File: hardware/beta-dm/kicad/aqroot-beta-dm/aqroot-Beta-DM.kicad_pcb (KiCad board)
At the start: 4 copper layers, 74 x 155 mm, 188 parts, among them J1 CH280QV10-CT_50P, J2 Molex_5025700893, J3 USB_C_Receptacle_USB2.0_16P, J4 JST-PH-2 BATTERY, J5 COMMUNITY_HEADER_2x13, J6 JST-PH-2 SPEAKER, Q1 AO3400A, SW1 BOOT, SW2 UP, SW3 DOWN, SW4 LEFT, SW5 RIGHT, SW6 A_SELECT, SW7 B_BACK, SW8 HOME, SW9 SW_SPDT, U1 ESP32-S3-WROOM-1, U10 USBLC6-2SC6, U11 BQ25185, U12 TPS63020, U13 TPS61023, U14 MAX17048, U15 TPS22918, U16 TCA9517ADGK, U17 TPS61169DCKR, U2 TCA9535PWR, U3 TCA9535PWR, U4 BMI270, U5 MAX98357A, U6 TSOP38238, U7 E07-400M10S, U8 E22-900M22S, U9 ST25R3916-AQET

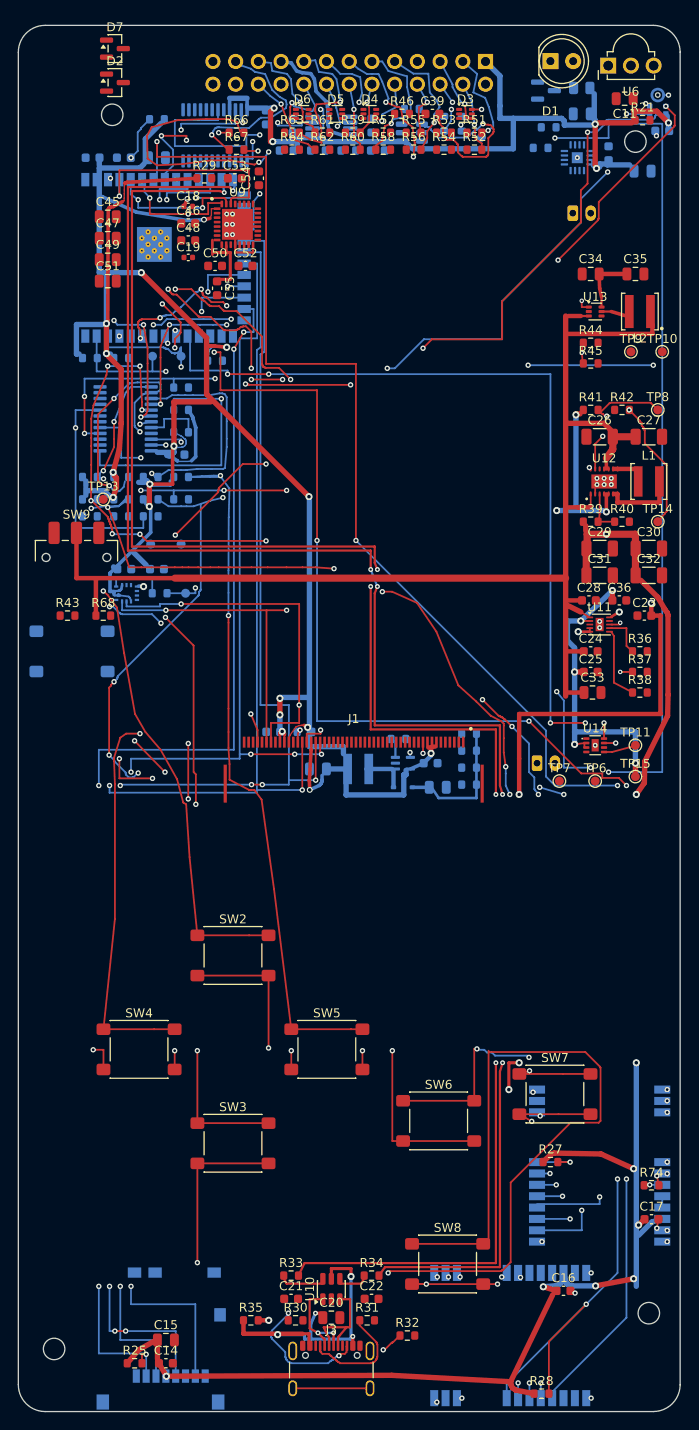
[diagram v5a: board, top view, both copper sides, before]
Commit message: hardware(beta-dm): GND stitching for the USB-C connector, the MCU and the switches
Copper. Only hardware/beta-dm/ is touched. Still no pours.

9 further stitches on grounds that gate a demo function rather than waiting for
the pour to find them:

  J3.A12   USB-C connector ground
  U1.1, U1.40   ESP32-S3 module grounds
  SW1.2    BOOT switch return
  R30.2, R31.2  the two 5.1k CC pull-downs - without these the Rd termination
                has no return and USB-C sink detection does not work
  R32.2    the 0R shield tie
  C1.1     the EN reset capacitor return
  R42.1    the PS_SYNC 0R tie to GND

Stub lengths 0.525-0.810 mm.

J3.B12 could not be stitched: no legal via site within 3.6 mm of it, the
connector corner is fully enclosed. It is an F.Cu ground pad, so the F.Cu pour
will pick it up when pours are created; it is recorded rather than forced.

Result: GND endpoints now 0 at U1, R30, R31, R32, C1 and R42; J3 1 (B12) and
SW1 2 remain for the pour. Board unconnected 239 -> 230.

Note on why these matter beyond tidiness. R30 and R31 are the USB-C CC
terminations - a 5.1k Rd with no ground return is not an Rd, and a source would
never see the sink. C1 is the ESP32-S3 reset capacitor and R42 ties the TPS63020
mode pin low; both are pull-to-ground parts whose function is exactly the
ground connection.

Verification: exact analytic validation - 0 violations, minimum separation
0.200 mm. Zones refilled through pcbnew, DRC 0 errors and 240 warnings with the
composition unchanged. Object-level preservation diff: 9 segments and 9 vias
added, 0 changes to footprints, pads, zones or Edge.Cuts. UUID prefix 9d54ba00,
verified absent before writing.

BETA FULL DIRECTORY: UNCHANGED.

Co-Authored-By: Claude Opus 5 <noreply@anthropic.com>
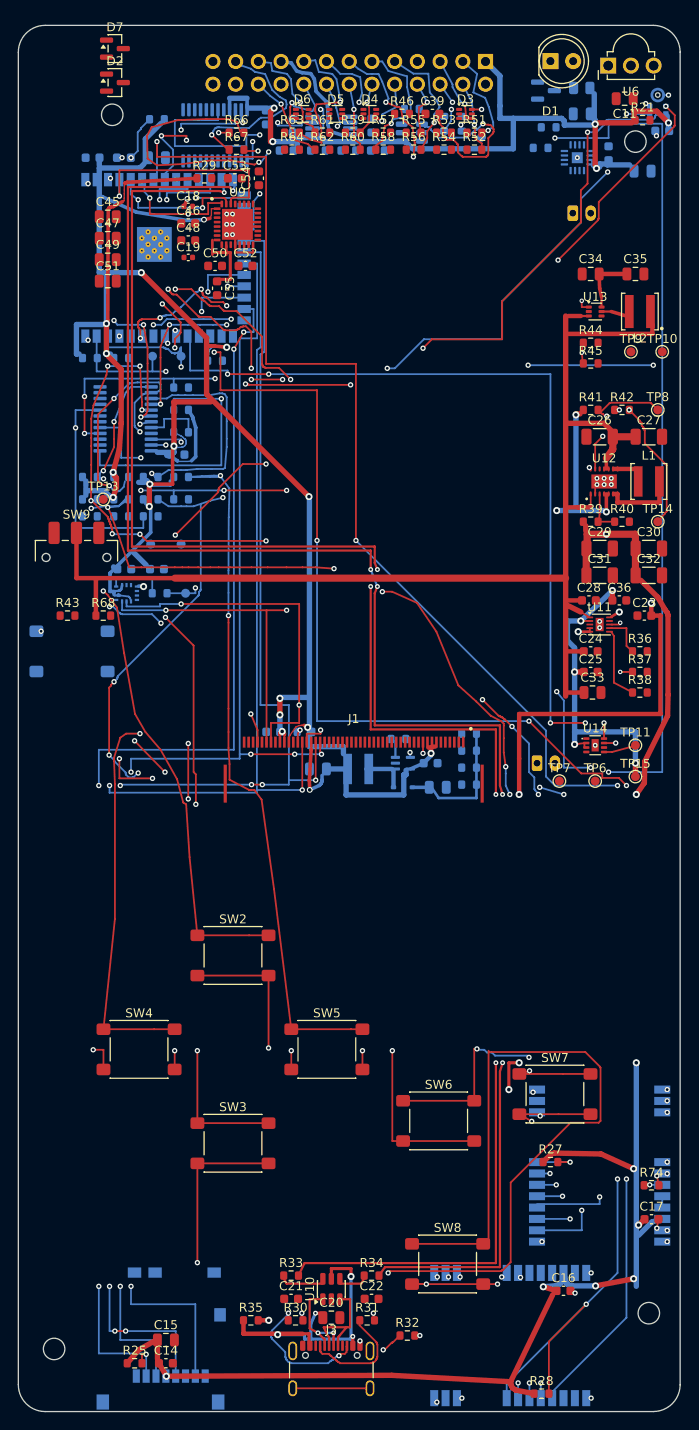
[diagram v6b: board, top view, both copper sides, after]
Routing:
- net GND: track 106.9 -> 112.4 mm, vias 52 -> 61
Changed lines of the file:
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@@
 	(footprint "C_0603_1608Metric"
 		(layer "B.Cu")
-		(at 28.5 79 180)
+		(at 46.1 82.5)
 		(descr "Capacitor SMD 0603 (1608 Metric), square (rectangular) end terminal, IPC-7351 nominal, (Body size source: IPC-SM-782 page 76, https://www.pcb-3d.com/wordpress/wp-content/uploads/ipc-sm-782a_amendment_1_and_2.pdf)")
 		(tags "capacitor")
-		(property "Reference" "C13"
-			(at 0 1.43 0)
+		(property "Reference" "C56"
+			(at 0 1.43 180)
 			(layer "B.SilkS")
 			(effects
@@
 			)
 		)
-		(property "Value" "100nF"
-			(at 0 -1.43 0)
+		(property "Value" "1uF"
+			(at 0 -1.43 180)
 			(layer "B.Fab")
 			(effects
@@
 		)
 		(property "Datasheet" ""
-			(at 0 0 0)
+			(at 0 0 180)
 			(layer "B.Fab")
 			(hide yes)
@@
 		)
 		(property "Description" ""
-			(at 0 0 0)
+			(at 0 0 180)
 			(layer "B.Fab")
 			(hide yes)
@@
 		)
 		(property "KiLib_Generator" "SMD_2terminal_chip_molded"
-			(at 0 0 0)
+			(at 0 0 180)
 			(layer "B.SilkS")
 			(hide yes)
@@
 		(duplicate_pad_numbers_are_jumpers no)
 		(fp_line
-			(start -0.14058 0.51)
-			(end 0.14058 0.51)
+			(start -0.14058 -0.51)
+			(end 0.14058 -0.51)
 			(stroke
 				(width 0.12)
@@
 		)
 		(fp_line
-			(start -0.14058 -0.51)
-			(end 0.14058 -0.51)
+			(start -0.14058 0.51)
+			(end 0.14058 0.51)
 			(stroke
 				(width 0.12)
@@
 		)
 		(fp_text user "${REFERENCE}"
-			(at 0 0 0)
+			(at 0 0 180)
 			(layer "B.Fab")
 			(effects
@@
 		)
 		(pad "1" smd roundrect
-			(at -0.775 0 180)
+			(at -0.775 0)
 			(size 0.9 0.95)
 			(layers "B.Cu" "B.Mask" "B.Paste")
@@
 		)
 		(pad "2" smd roundrect
-			(at 0.775 0 180)
+			(at 0.775 0)
 			(size 0.9 0.95)
 			(layers "B.Cu" "B.Mask" "B.Paste")
@@
 	(footprint "C_0603_1608Metric"
 		(layer "B.Cu")
-		(at 46.1 82.5)
+		(at 28.5 79 180)
 		(descr "Capacitor SMD 0603 (1608 Metric), square (rectangular) end terminal, IPC-7351 nominal, (Body size source: IPC-SM-782 page 76, https://www.pcb-3d.com/wordpress/wp-content/uploads/ipc-sm-782a_amendment_1_and_2.pdf)")
 		(tags "capacitor")
-		(property "Reference" "C56"
-			(at 0 1.43 180)
+		(property "Reference" "C13"
+			(at 0 1.43 0)
 			(layer "B.SilkS")
 			(effects
@@
 			)
 		)
-		(property "Value" "1uF"
-			(at 0 -1.43 180)
+		(property "Value" "100nF"
+			(at 0 -1.43 0)
 			(layer "B.Fab")
 			(effects
@@
 		)
 		(property "Datasheet" ""
-			(at 0 0 180)
+			(at 0 0 0)
 			(layer "B.Fab")
 			(hide yes)
@@
 		)
 		(property "Description" ""
-			(at 0 0 180)
+			(at 0 0 0)
 			(layer "B.Fab")
 			(hide yes)
@@
 		)
 		(property "KiLib_Generator" "SMD_2terminal_chip_molded"
-			(at 0 0 180)
+			(at 0 0 0)
 			(layer "B.SilkS")
 			(hide yes)
@@
 		(duplicate_pad_numbers_are_jumpers no)
 		(fp_line
-			(start -0.14058 -0.51)
-			(end 0.14058 -0.51)
+			(start -0.14058 0.51)
+			(end 0.14058 0.51)
 			(stroke
 				(width 0.12)
@@
 		)
 		(fp_line
-			(start -0.14058 0.51)
-			(end 0.14058 0.51)
+			(start -0.14058 -0.51)
+			(end 0.14058 -0.51)
 			(stroke
 				(width 0.12)
@@
 		)
 		(fp_text user "${REFERENCE}"
-			(at 0 0 180)
+			(at 0 0 0)
 			(layer "B.Fab")
 			(effects
@@
 		)
 		(pad "1" smd roundrect
-			(at -0.775 0)
+			(at -0.775 0 180)
 			(size 0.9 0.95)
 			(layers "B.Cu" "B.Mask" "B.Paste")
@@
 		)
 		(pad "2" smd roundrect
-			(at 0.775 0)
+			(at 0.775 0 180)
 			(size 0.9 0.95)
 			(layers "B.Cu" "B.Mask" "B.Paste")
@@
 	)
 	(segment
+		(start 66.675 43)
+		(end 67.2 43)
+		(width 0.2)
+		(layer "F.Cu")
+		(net "GND")
+	)
+	(segment
+		(start 39.825 144.8)
+		(end 39.7 144)
+		(width 0.2)
+		(layer "F.Cu")
+		(net "GND")
+	)
+	(segment
+		(start 44.325 146.5)
+		(end 44.9 146.5)
+		(width 0.2)
+		(layer "F.Cu")
+		(net "GND")
+	)
+	(segment
+		(start 38.2 147.645)
+		(end 38.2 147.1)
+		(width 0.2)
+		(layer "F.Cu")
+		(net "GND")
+	)
+	(segment
+		(start 31.825 144.8)
+		(end 31.7 144)
+		(width 0.2)
+		(layer "F.Cu")
+		(net "GND")
+	)
+	(segment
 		(start 56.02 121.75)
 		(end 60.4015 121.75)
@@
 	)
 	(via
+		(at 67.2 43)
+		(size 0.6)
+		(drill 0.3)
+		(layers "F.Cu" "B.Cu")
+		(net "GND")
+	)
+	(via
+		(at 31.7 144)
+		(size 0.6)
+		(drill 0.3)
+		(layers "F.Cu" "B.Cu")
+		(net "GND")
+	)
+	(via
+		(at 7.8 35.2)
+		(size 0.6)
+		(drill 0.3)
+		(layers "F.Cu" "B.Cu")
+		(net "GND")
+	)
+	(via
+		(at 7.8 17.7)
+		(size 0.6)
+		(drill 0.3)
+		(layers "F.Cu" "B.Cu")
+		(net "GND")
+	)
+	(via
+		(at 38.2 147.1)
+		(size 0.6)
+		(drill 0.3)
+		(layers "F.Cu" "B.Cu")
+		(net "GND")
+	)
+	(via
+		(at 39.7 144)
+		(size 0.6)
+		(drill 0.3)
+		(layers "F.Cu" "B.Cu")
+		(net "GND")
+	)
+	(via
+		(at 11.6 14.8)
+		(size 0.6)
+		(drill 0.3)
+		(layers "F.Cu" "B.Cu")
+		(net "GND")
+	)
+	(via
+		(at 44.9 146.5)
+		(size 0.6)
+		(drill 0.3)
+		(layers "F.Cu" "B.Cu")
+		(net "GND")
+	)
+	(via
+		(at 2.55 67.75)
+		(size 0.6)
+		(drill 0.3)
+		(layers "F.Cu" "B.Cu")
+		(net "GND")
+	)
+	(via
 		(at 65.5 50.65)
 		(size 0.55)
@@
 		(width 0.2)
 		(layer "B.Cu")
+		(net "GND")
+	)
+	(segment
+		(start 7.49 17.25)
+		(end 7.8 17.7)
+		(width 0.2)
+		(layer "B.Cu")
+		(net "GND")
+	)
+	(segment
+		(start 11.025 14.8)
+		(end 11.6 14.8)
+		(width 0.2)
+		(layer "B.Cu")
+		(net "GND")
+	)
+	(segment
+		(start 2.02 67.75)
+		(end 2.55 67.75)
+		(width 0.2)
+		(layer "B.Cu")
+		(net "GND")
+	)
+	(segment
+		(start 7.49 34.75)
+		(end 7.8 35.2)
+		(width 0.2)
+		(layer "B.Cu")

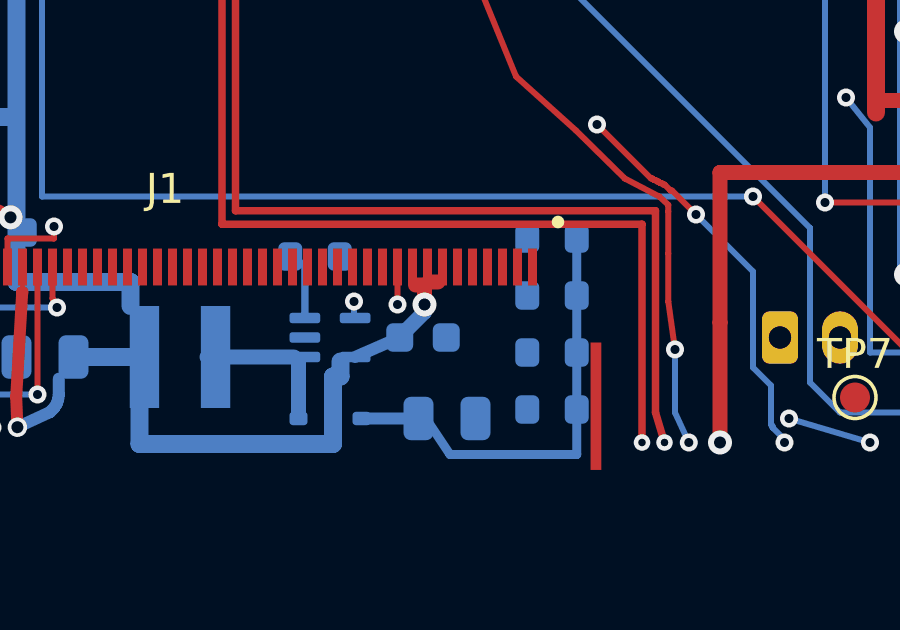
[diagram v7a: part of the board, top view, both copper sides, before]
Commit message: hardware(beta-dm): display backlight routed, two local 0.250 mm E6 areas
CONDITIONS FIRST, per the ruling.

TPS61169 OVP, from TI SNVSA40B (rev June 2024), the datasheet the schematic
already cites: VOVP_SW = 36 V min / 37.5 V typ / 39 V max; VREF = 188 / 204 /
220 mV; SW absolute maximum 40 V; recommended VOUT max 38 V. Open-LED
protection latches the part off after 3 switching cycles and the output then
falls to VIN, so 39 V is a transient ceiling, not a sustained rail. WORST-CASE
VOLTAGE BASIS USED FOR SPACING: 39 V.

Normal operation, from the topology: 204 mV / 2.55 R = 80 mA total, 20 mA per
branch through the 39 R ballasts, LED_BOOST = Vf + 0.780 + 0.204 =
3.884-4.484 V.

C44 IS RATED. The pass-4 document said it had no voltage rating; that was
wrong and is corrected here. The schematic carries Voltage = 50V,
Dielectric = X7R on C44, with a property note explaining that the rating is
set by VOVP_SW and not by the ~4.2 V normal output. 50 V vs 39 V = 1.28x. The
BOM export simply does not include the Voltage field.

0.250 mm against 39 V: IPC-2221 B4 (external, permanent polymer coating) asks
0.13 mm in the 31-50 V band -> 1.92x. In the 0-15 V operating band it asks
0.05 mm -> 5.0x. JLCPCB 4-layer minimum spacing 0.09 mm -> 2.78x. For scale,
the E6 pockets already ratified on this board run at 0.100-0.160 mm.

IMPLEMENTATION

  net        margin        seg via   length
  LED_A1     0.30 global     3   1    4.874 mm
  LED_A2     0.250 local     5   1    3.211 mm
  LED_A3     0.250 local     4   1    2.957 mm
  LED_A4     0.250 local    11   1    5.130 mm
  LED_K      0.250 local    31   1   15.400 mm
  LED_BOOST  0.30 global     2   0    3.800 mm

All six ONE ISLAND each by KiCad's own connectivity. 56 segments, 5 vias,
35.372 mm. Measured minimum clearance in the landed geometry: 0.2500 mm
exactly - not below the rule figure.

Two scoped areas, both minimal and both verified to WHOLLY enclose every
object that needs them (>= 0.075 mm overhang past the copper):
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
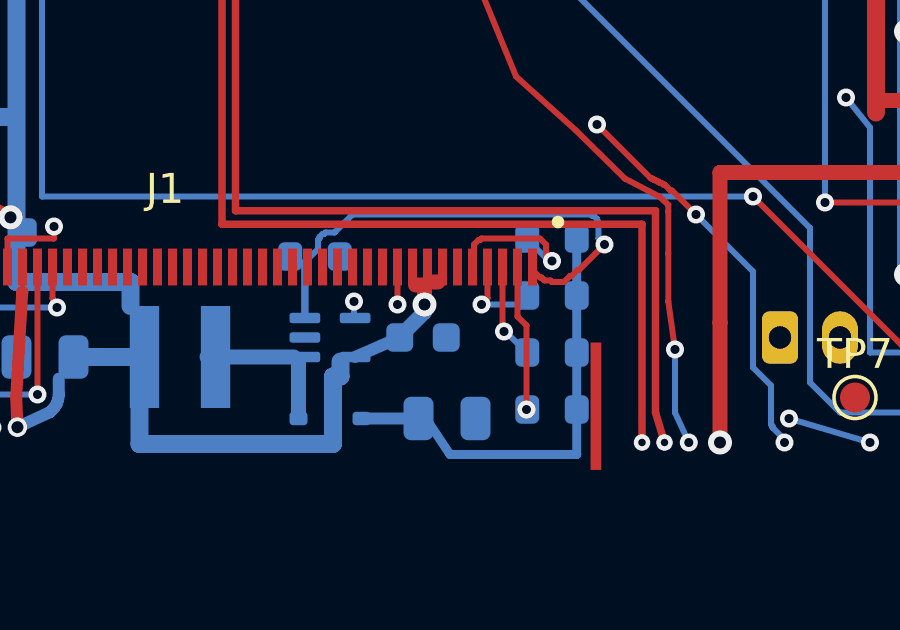
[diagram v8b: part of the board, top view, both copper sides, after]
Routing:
- net /03_SPI_A_DISPLAY_SD/LED_K: track 1.85 -> 17.2 mm, vias 0 -> 1
- net /03_SPI_A_DISPLAY_SD/LED_A4: track 0.00 -> 5.13 mm, vias 0 -> 1
- net /03_SPI_A_DISPLAY_SD/LED_A1: track 0.00 -> 4.87 mm, vias 0 -> 1
- net /03_SPI_A_DISPLAY_SD/LED_BOOST: track 14.7 -> 18.5 mm
- net /03_SPI_A_DISPLAY_SD/LED_A2: track 0.00 -> 3.21 mm, vias 0 -> 1
- net /03_SPI_A_DISPLAY_SD/LED_A3: track 0.00 -> 2.96 mm, vias 0 -> 1
